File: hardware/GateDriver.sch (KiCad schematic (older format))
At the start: 9 parts

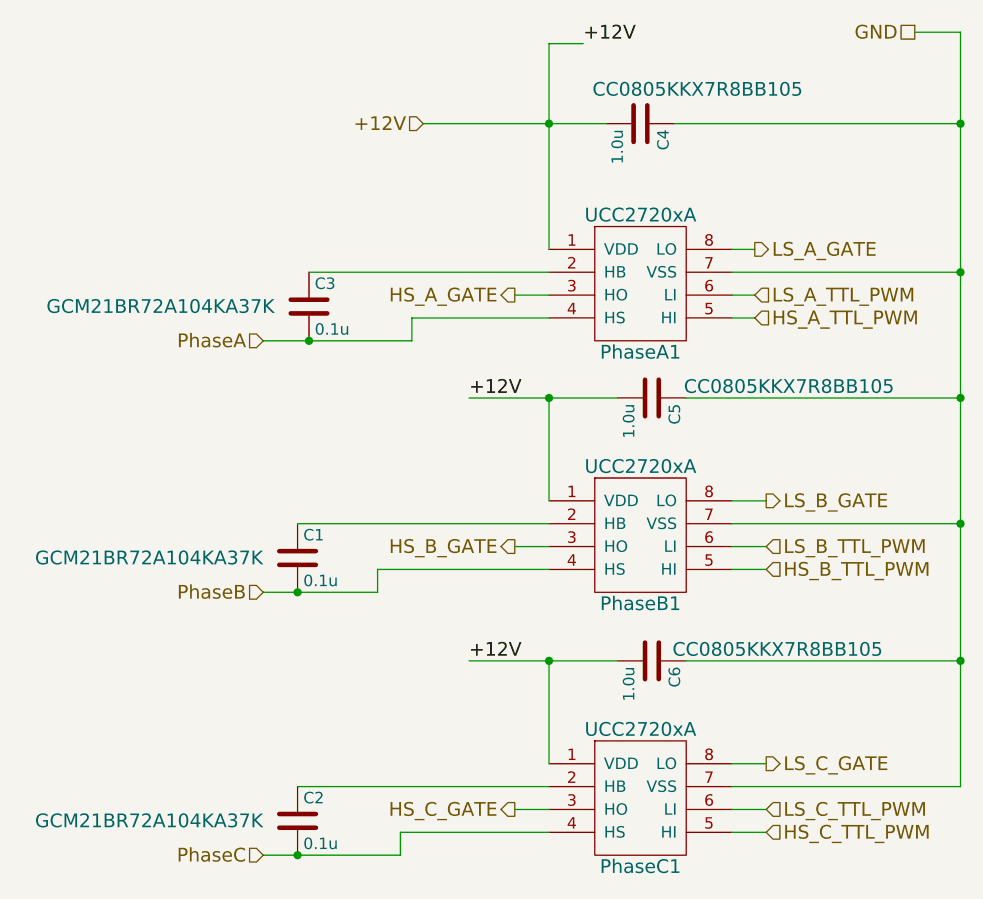
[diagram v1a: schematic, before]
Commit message: updated part numbers
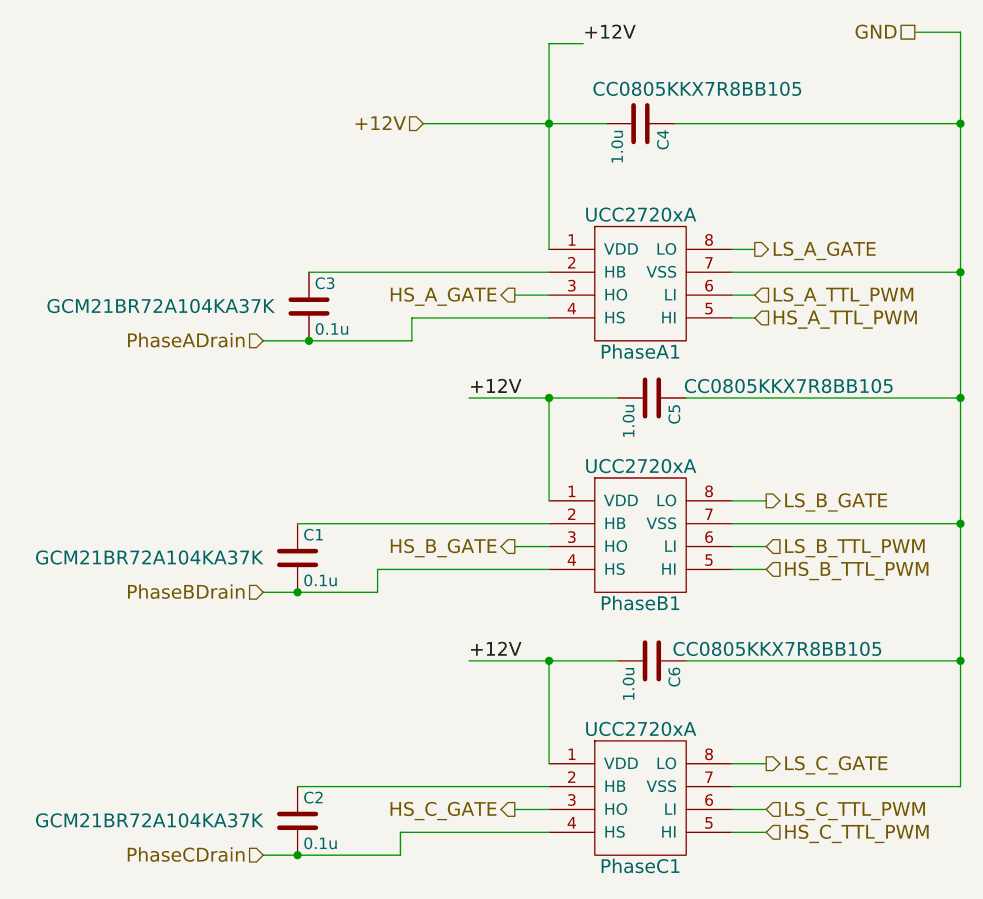
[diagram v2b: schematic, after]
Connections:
- net PhaseA renamed PhaseADrain
- net PhaseB renamed PhaseBDrain
- net PhaseC renamed PhaseCDrain
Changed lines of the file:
@@
 LIBS:crf_1
 LIBS:STM32F4-DISCOVERY-SIMON
+LIBS:bldc_v1-cache
 EELAYER 25 0
 EELAYER END
@@
 $EndComp
 Text HLabel 2250 2250 0    60   Input ~ 0
-PhaseA
+PhaseADrain
 Text HLabel 2250 3350 0    60   Input ~ 0
-PhaseB
+PhaseBDrain
 Text HLabel 2250 4500 0    60   Input ~ 0
-PhaseC
+PhaseCDrain
 Text HLabel 5100 900  0    60   UnSpc ~ 0
 GND

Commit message: Converted to kicad 5
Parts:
- C1, C2, C3, C4, C5, C6: symbol C -> Device:C
- PhaseA1, PhaseB1, PhaseC1: symbol UCC2720xA -> infineon:UCC2720xA
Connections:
- net PhaseADrain renamed PhaseASource
- net PhaseBDrain renamed PhaseBSource
- net PhaseCDrain renamed PhaseCSource
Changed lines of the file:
@@
-EESchema Schematic File Version 2
-LIBS:power
-LIBS:device
-LIBS:switches
-LIBS:relays
-LIBS:motors
-LIBS:transistors
-LIBS:conn
-LIBS:linear
-LIBS:regul
-LIBS:74xx
-LIBS:cmos4000
-LIBS:adc-dac
-LIBS:memory
-LIBS:xilinx
-LIBS:microcontrollers
-LIBS:dsp
-LIBS:microchip
-LIBS:analog_switches
-LIBS:motorola
-LIBS:texas
-LIBS:intel
-LIBS:audio
-LIBS:interface
-LIBS:digital-audio
-LIBS:philips
-LIBS:display
-LIBS:cypress
-LIBS:siliconi
-LIBS:opto
-LIBS:atmel
-LIBS:contrib
-LIBS:valves
-LIBS:infineon
-LIBS:crf_1
-LIBS:STM32F4-DISCOVERY-SIMON
-LIBS:bldc_v1-cache
-EELAYER 25 0
+EESchema Schematic File Version 4
+EELAYER 26 0
 EELAYER END
 $Descr A4 11693 8268
@@
 $EndDescr
 $Comp
-L UCC2720xA PhaseA1
+L infineon:UCC2720xA PhaseA1
 U 1 1 5AAF1479
 P 3800 1900
@@
 $EndComp
 $Comp
-L UCC2720xA PhaseB1
+L infineon:UCC2720xA PhaseB1
 U 1 1 5AAF151B
 P 3800 3000
@@
 $EndComp
 $Comp
-L UCC2720xA PhaseC1
+L infineon:UCC2720xA PhaseC1
 U 1 1 5AAF1572
 P 3800 4150
@@
 $EndComp
 $Comp
-L C C3
+L Device:C C3
 U 1 1 5AAF19CF
 P 2450 2100
@@
 $EndComp
 $Comp
-L C C1
+L Device:C C1
 U 1 1 5AAF1A5A
 P 2400 3200
@@
 $EndComp
 $Comp
-L C C2
+L Device:C C2
 U 1 1 5AAF1AF9
 P 2400 4350
@@
 $EndComp
 Text HLabel 2250 2250 0    60   Input ~ 0
-PhaseADrain
+PhaseASource
 Text HLabel 2250 3350 0    60   Input ~ 0
-PhaseBDrain
+PhaseBSource
 Text HLabel 2250 4500 0    60   Input ~ 0
-PhaseCDrain
+PhaseCSource
 Text HLabel 5100 900  0    60   UnSpc ~ 0
 GND
@@
 	3500 2050 3350 2050
 Wire Wire Line
-	2250 2250 2900 2250
+	2250 2250 2450 2250
 Wire Wire Line
 	3500 2150 2900 2150
@@
 	2400 3050 3500 3050
 Wire Wire Line
-	2250 4500 2850 4500
+	2250 4500 2400 4500
 Wire Wire Line
 	2850 4500 2850 4400
@@
 	2400 4200 3500 4200
 Wire Wire Line
-	2250 3350 2750 3350
+	2250 3350 2400 3350
 Wire Wire Line
 	2750 3350 2750 3250
@@
 	4300 4100 4450 4100
 Wire Wire Line
-	5300 900  5300 4200
+	5300 900  5300 1300
 Wire Wire Line
 	5300 1950 4300 1950
@@
 Connection ~ 5300 3050
 $Comp
-L C C4
+L Device:C C4
 U 1 1 5AAF26C0
 P 3900 1300
@@
 Connection ~ 5300 1300
 Wire Wire Line
-	2950 1300 3750 1300
-Wire Wire Line
-	3500 950  3500 1850
-$Comp
-L C C5
+	2950 1300 3500 1300
+Wire Wire Line
+	3500 950  3500 1300
+$Comp
+L Device:C C5
 U 1 1 5AAF28D3
 P 3950 2500
@@
 Connection ~ 5300 2500
 Wire Wire Line
-	3150 2500 3800 2500
+	3150 2500 3500 2500
 Wire Wire Line
 	3500 2500 3500 2950
 $Comp
-L C C6
+L Device:C C6
 U 1 1 5AAF29AA
 P 3950 3650
@@
 	3500 4100 3500 3650
 Wire Wire Line
-	3150 3650 3800 3650
+	3150 3650 3500 3650
 Text HLabel 4400 2050 2    60   Input ~ 0
 LS_A_TTL_PWM
@@
 Text Label 3150 3650 0    60   ~ 0
 +12V
+Wire Wire Line
+	2450 2250 2900 2250
+Wire Wire Line
+	2400 3350 2750 3350
+Wire Wire Line
+	2400 4500 2850 4500
+Wire Wire Line
+	5300 1950 5300 2500
+Wire Wire Line
+	5300 3050 5300 3650
+Wire Wire Line
+	5300 1300 5300 1950
+Wire Wire Line
+	5300 2500 5300 3050
+Wire Wire Line
+	5300 3650 5300 4200
+Wire Wire Line
+	3500 1300 3750 1300
+Wire Wire Line
+	3500 1300 3500 1850
+Wire Wire Line
+	3500 2500 3800 2500
+Wire Wire Line
+	3500 3650 3800 3650
 $EndSCHEMATC
